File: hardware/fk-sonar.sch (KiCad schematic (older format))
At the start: 46 parts, among them J1 MICRO-USB, J2 Conn_01x03, J3 CONN_01X06, J6 CONN-HDR-2x5, M1 MOUNT_HOLE, M2 MOUNT_HOLE, M3 MOUNT_HOLE, M4 MOUNT_HOLE, Q1 2N7002LT1G, Q2 2N7002LT1G, Q3 2N7002LT1G, Q4 2N7002LT1G, SW1 SPNO, U1 ATSAMD21G18A-AU, U2 MCP1700T-XXX2E, Y1 FC-135

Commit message: Copying fk-core, actually and dropping GPS/SD/etc.
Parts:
- removed D4: PRTR5V0U2X, RocketScreamKicadLibrary:SOT-143B, symbol PRTR5V0U2X
- removed D5: Orange, RocketScreamKicadLibrary:LED-0603, symbol LED-SINGLE
- removed J1: MICRO-USB, conservify:MICRO-USB, symbol MICRO-USB
- removed J2: Conn_01x03, Socket_Strips:Socket_Strip_Straight_1x03_Pitch2.54mm, symbol Conn_01x03
- removed J3: CONN_01X06, Socket_Strips:Socket_Strip_Straight_1x06_Pitch2.54mm, symbol CONN_01X06
- removed J6: CONN-HDR-2x5, Socket_Strips:Socket_Strip_Straight_2x05_Pitch1.27mm_SMD, symbol CONN-HDR-2x5
- removed M2: MOUNT_HOLE, RocketScreamKicadLibrary:HOLE_NPTH_2.2MM, symbol MOUNT_HOLE
- removed U2: MCP1700T-XXX2E, RocketScreamKicadLibrary:SOT-89, symbol MCP1700T-XXX2E
- added C13, C20: 100nF, RocketScreamKicadLibrary:CAP-0603, symbol CAPACITOR-CERAMIC
- added C15, C16: 4.7uF 10V X5R, RocketScreamKicadLibrary:CAP-0603, symbol CAPACITOR-CERAMIC
- added C17, C19, C21: 1uF 10V X5R, RocketScreamKicadLibrary:CAP-0603, symbol CAPACITOR-CERAMIC
- added C18: 10nF, RocketScreamKicadLibrary:CAP-0603, symbol CAPACITOR-CERAMIC
- added D4: Blue, RocketScreamKicadLibrary:LED-0603, symbol LED-SINGLE
- added D5: PMEG3020CPA, RocketScreamKicadLibrary:SOT-1016, symbol DIODE_DUAL_Schottky
- added D6: PRTR5V0U2X, RocketScreamKicadLibrary:SOT-143B, symbol PRTR5V0U2X
- added D7: Green, RocketScreamKicadLibrary:LED-0603, symbol LED-SINGLE
- added D8: Red, RocketScreamKicadLibrary:LED-0603, symbol LED-SINGLE
- added J1: Conn_01x03, Socket_Strips:Socket_Strip_Straight_1x03_Pitch2.54mm, symbol Conn_01x03
- added J2: CONN-HDR-2x5, Socket_Strips:Socket_Strip_Straight_2x05_Pitch1.27mm_SMD, symbol CONN-HDR-2x5
- added J3: RF-SMA-EDGE, RocketScreamKicadLibrary:RF-SMA-EDGE, symbol RF-SMA-EDGE
- added J4: MICRO-USB, RocketScreamKicadLibrary:MICRO-USB, symbol MICRO-USB
- added J5: S2B-PH-SM4-TB, RocketScreamKicadLibrary:S2B-PH-SM4-TB, symbol S2B-PH-SM4-TB
- added M2, M5: FIDUCIAL, RocketScreamKicadLibrary:FIDUCIAL-1MM, symbol FIDUCIAL
- added M6: MOUNT_HOLE, RocketScreamKicadLibrary:HOLE_NPTH_2.2MM, symbol MOUNT_HOLE
- added R11, R6: 2K2, RocketScreamKicadLibrary:RES-0603, symbol RESISTOR
- added R12: 330R, RocketScreamKicadLibrary:RES-0603, symbol RESISTOR
- added R13: 1M, RocketScreamKicadLibrary:RES-0603, symbol RESISTOR
- added R14, R15: 4.7K, RocketScreamKicadLibrary:RES-0603, symbol RESISTOR
- added R16, R18: 10K, RocketScreamKicadLibrary:RES-0603, symbol RESISTOR
- added R19: 1k, RocketScreamKicadLibrary:RES-0603, symbol RESISTOR
- added R20: 180R, RocketScreamKicadLibrary:RES-0603, symbol RESISTOR
- added R7: 1K18, RocketScreamKicadLibrary:RES-0603, symbol RESISTOR
- added U2: RFM95W, RocketScreamKicadLibrary:RFM9xW, symbol RFM9xW
- added U3: BQ24074RGTT, RocketScreamKicadLibrary:QFN-16_3x3mm, symbol BQ24074
- added U4: S25FL116K0XMFI041, RocketScreamKicadLibrary:SOIC-8-N, symbol S25FL1xxK0XM
- added U5: MAX1704XX, Housings_DFN_QFN:DFN-8-1EP_3x2mm_Pitch0.5mm, symbol MAX1704XX
- added U6: MCP1700T-3302E/MB, RocketScreamKicadLibrary:SOT-89, symbol MCP1700T-XXX2E
- C1: value 18pF -> 4.7uF 10V X5R; footprint Capacitors_SMD:C_0603_HandSoldering -> RocketScreamKicadLibrary:CAP-0603; price 0 -> 0.71; spn1 581-06035A180J -> 581-0603ZD475MAT2A
- C10: value 4.7nF -> 4.7uF 10V X5R; footprint Capacitors_SMD:C_0603_HandSoldering -> RocketScreamKicadLibrary:CAP-0603; price 0 -> 0.71; spn1 80-C0603C472K9R -> 581-0603ZD475MAT2A
- C11: value 1uF -> 1uF 50V X5R; footprint Capacitors_SMD:C_0603_HandSoldering -> RocketScreamKicadLibrary:CAP-0603; price 0 -> 0.32
- C12: value 1uF -> 47uF 10V X5R; footprint Capacitors_SMD:C_0603_HandSoldering -> RocketScreamKicadLibrary:CAP-0603; price 0 -> 0.53; spn1 963-UMK107BJ105KA-T -> 81-GRM188R60J476ME5D
- C14: value 4.7uF 10V X5R -> 4.7nF 25V X7R; footprint Capacitors_SMD:C_0603_HandSoldering -> RocketScreamKicadLibrary:CAP-0603; price 0 -> 0.1; spn1 581-0603ZD475MAT2A -> 603-AC603KRX7R8BB472
- C2: value 18pF -> 100nF; footprint Capacitors_SMD:C_0603_HandSoldering -> RocketScreamKicadLibrary:CAP-0603; price 0 -> 0.1; spn1 581-06035A180J -> 81-GRM39X104K50D
- C3, C4: value 100nF -> 18pF; footprint Capacitors_SMD:C_0603_HandSoldering -> RocketScreamKicadLibrary:CAP-0603; price 0 -> 0.1; spn1 81-GRM39X104K50D -> 581-06035A180J
- C5: value 1uF 10V X5R -> 100nF; footprint Capacitors_SMD:C_0603_HandSoldering -> RocketScreamKicadLibrary:CAP-0603; price 0 -> 0.1; spn1 581-0603YD105K -> 81-GRM39X104K50D
- C6: value 100nF -> 1uF 10V X5R; footprint Capacitors_SMD:C_0603_HandSoldering -> RocketScreamKicadLibrary:CAP-0603; price 0 -> 0.1; spn1 81-GRM39X104K50D -> 581-0603YD105K
- C7, C8: footprint Capacitors_SMD:C_0603_HandSoldering -> RocketScreamKicadLibrary:CAP-0603; price 0 -> 0.1
- C9: value 4.7uF -> 100nF; footprint Capacitors_SMD:C_0603_HandSoldering -> RocketScreamKicadLibrary:CAP-0603; price 0 -> 0.1; spn1 581-0603ZD475MAT2A -> 81-GRM39X104K50D
- D1: price 0 -> 0.26
- D2: value Yellow -> Orange; price 0 -> 0.26; spn1 859-LTST-C190KSKT -> 859-LTST-C190KFKT
- D3: value Blue -> Yellow; price 0 -> 0.3; spn1 859-LTST-C191TBKT -> 859-LTST-C190KSKT
- F1: price 0 -> 0.33
- L1, L2: value BLM18KG221SN1D -> BKP1005TS121-T; footprint Inductors_SMD:L_0603_HandSoldering -> RocketScreamKicadLibrary:IND-0603; price 0 -> 0.1; spn1 81-BLM18KG221SN1D -> 963-BKP1608HS121-T
- M1, M3, M4: price 0 -> (none)
- Q1, Q2, Q3, Q4: price 0 -> 0.14
- R1, R17, R5: value 2k2 -> 2K2; footprint Resistors_SMD:R_0603_HandSoldering -> RocketScreamKicadLibrary:RES-0603; price 0 -> 0.1
- R10: value 1M -> 2K94; footprint Resistors_SMD:R_0603_HandSoldering -> RocketScreamKicadLibrary:RES-0603; price 0 -> 0.38; spn1 603-RC0603FR-071ML -> 667-ERJ-S03F2941V
- R2: value 330R -> 10K; footprint Resistors_SMD:R_0603_HandSoldering -> RocketScreamKicadLibrary:RES-0603; price 0 -> 0.1; spn1 603-RC0603FR-07330RL -> 603-RC0603FR-0710KL
- R3: value 2k2 -> 330R; footprint Resistors_SMD:R_0603_HandSoldering -> RocketScreamKicadLibrary:RES-0603; price 0 -> 0.1; spn1 603-RC0603FR-072K2L -> 603-RC0603FR-07330RL
- R4: value 10K -> 2K2; footprint Resistors_SMD:R_0603_HandSoldering -> RocketScreamKicadLibrary:RES-0603; price 0 -> 0.1; spn1 603-RC0603FR-0710KL -> 603-RC0603FR-072K2L
- R8: value 100k -> 46K4; footprint Resistors_SMD:R_0603_HandSoldering -> RocketScreamKicadLibrary:RES-0603; price 0 -> 0.15; spn1 603-RC0603FR-07100KL -> 667-ERJ-3EKF4642V
- R9: value 330R -> 100K; footprint Resistors_SMD:R_0603_HandSoldering -> RocketScreamKicadLibrary:RES-0603; price 0 -> 0.1; spn1 603-RC0603FR-07330RL -> 603-RC0603FR-07100KL
- SW1: footprint RocketScreamKicadLibrary:TS-018 -> conservify:SW_SPST_WURTH_1; price 0 -> 0.55; supplier1 (none) -> digikey
- U1: price 0 -> 3.15
- Y1: price 0 -> 0.54
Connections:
- net labels added: CHG, PG, SD_CS, VBAT, VBUS, VEXT, VIN, WIFI_CS, WIFI_EN, WIFI_IRQ, WIFI_RST, WIFI_WAKE
- net labels removed: SCL2, SCL3, SDA2, SDA3, SENSOR
- wire segments 164 -> 273
- no-connect marks 7 -> 19
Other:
- note added: "1. All capacitors are NP0/COG 50V unless specified.\n2. All resistors are 62.5mW 1% unless specified."
- note added: "100mA"
- note added: "16Mbit = 2Mbytes"
- note added: "500mA"
- note added: "EN2 EN1"
- note added: "FIDUCIALS"
- note added: "HI HI"
- note added: "HI LOW"
- note added: "I-INPUT LIMIT"
- note added: "LED"
- note added: "LEDS"
- note added: "LOW HI"
- note added: "LOW LOW"
- note added: "MCU"
- note added: "MOUNTING"
- note added: "NOTES"
- note added: "POWER MANAGEMENT"
- note added: "RFM95W\n"
- note added: "SERIAL FLASH"
- note added: "SWD/JTAG"
- note added: "Set by R6:1.3A"
- note added: "Standby"
- note added: "USB-DEVICE"
- note added: "VIN:5-10.5V\n(OVP up to 28V)"

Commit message: The PCB.
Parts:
- added J6: Conn_01x04, Socket_Strips:Socket_Strip_Straight_1x04_Pitch2.54mm, symbol Conn_01x04
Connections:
- wire segments 273 -> 279
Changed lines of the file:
@@
 LIBS:conservify
 LIBS:fk-sonar-cache
-LIBS:fk-core-cache
 EELAYER 25 0
 EELAYER END
@@
 RESET
 Text Label 2000 7350 0    50   ~ 0
-D13
+A2
 Text Label 9900 6350 0    50   ~ 0
 USB-
@@
 LEDS
 Text Label 6950 6150 2    50   ~ 0
-A3
+A4
 Text Label 6950 6950 2    50   ~ 0
-A4
+A5
 Text Label 6950 7750 2    50   ~ 0
-A5
+D13
 Wire Wire Line
 	2800 2300 2500 2300
@@
 Wire Wire Line
 	3350 9050 3500 9050
+$Comp
+L Conn_01x04 J6
+U 1 1 5A1E0D62
+P 6450 4100
+F 0 "J6" H 6450 4300 50  0000 C CNN
+F 1 "Conn_01x04" H 6450 3800 50  0000 C CNN
+F 2 "Socket_Strips:Socket_Strip_Straight_1x04_Pitch2.54mm" H 6450 4100 50  0001 C CNN
+F 3 "" H 6450 4100 50  0001 C CNN
+	1    6450 4100
+	1    0    0    -1
+$EndComp
+$Comp
+L 3V3 #PWR069
+U 1 1 5A1E1F21
+P 6100 3950
+F 0 "#PWR069" H 6100 3800 50  0001 C CNN
+F 1 "3V3" H 6100 4090 50  0000 C CNN
+F 2 "" H 6100 3950 60  0000 C CNN
+F 3 "" H 6100 3950 60  0000 C CNN
+	1    6100 3950
+	1    0    0    -1
+$EndComp
+$Comp
+L GND #PWR070
+U 1 1 5A1E2010
+P 6100 4400
+F 0 "#PWR070" H 6100 4150 50  0001 C CNN
+F 1 "GND" H 6100 4250 50  0001 C CNN
+F 2 "" H 6100 4400 60  0000 C CNN
+F 3 "" H 6100 4400 60  0000 C CNN
+	1    6100 4400
+	1    0    0    -1
+$EndComp
+Wire Wire Line
+	6250 4000 6100 4000
+Wire Wire Line
+	6100 4000 6100 3950
+Wire Wire Line
+	6250 4300 6100 4300
+Wire Wire Line
+	6100 4300 6100 4400
+Text Label 6050 4100 0    50   ~ 0
+SDA
+Text Label 6050 4200 0    50   ~ 0
+SCL
+Wire Wire Line
+	6050 4200 6250 4200
+Wire Wire Line
+	6250 4100 6050 4100
 $EndSCHEMATC

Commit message: New SWD/JTAG programming footprint to avoid confusion.
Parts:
- J2: footprint Socket_Strips:Socket_Strip_Straight_2x05_Pitch1.27mm_SMD -> conservify:HDR_2x5_Pitch1.27mm_SMD_JTAG_SWD
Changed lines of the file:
@@
 F 0 "J2" H 6050 10250 60  0000 C CNN
 F 1 "CONN-HDR-2x5" H 6050 9500 60  0001 C CNN
-F 2 "Socket_Strips:Socket_Strip_Straight_2x05_Pitch1.27mm_SMD" H 6050 9400 60  0001 C CNN
+F 2 "conservify:HDR_2x5_Pitch1.27mm_SMD_JTAG_SWD" H 6050 9400 60  0001 C CNN
 F 3 "" H 6050 9750 60  0000 C CNN
 F 4 "0.73" H 6050 10350 50  0001 C CNN "price"

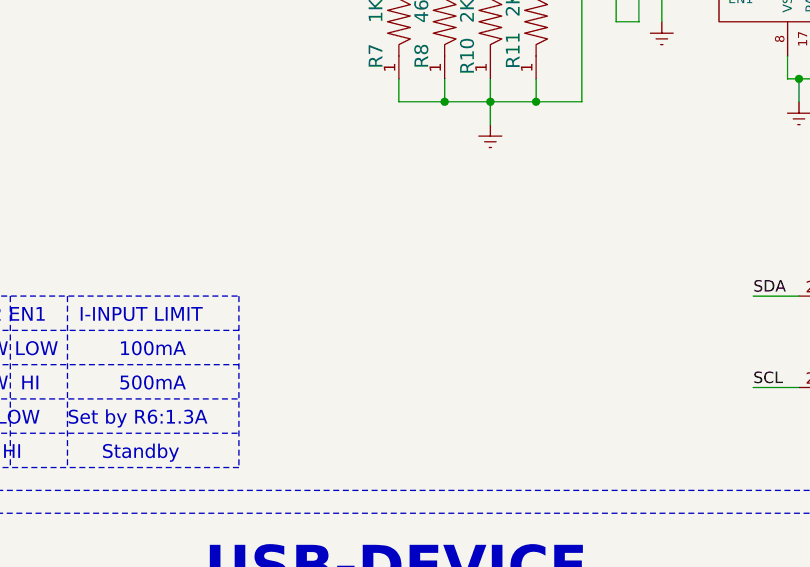
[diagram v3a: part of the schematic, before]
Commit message: Adding a solar panel connector. Just a JST below the battery JST.
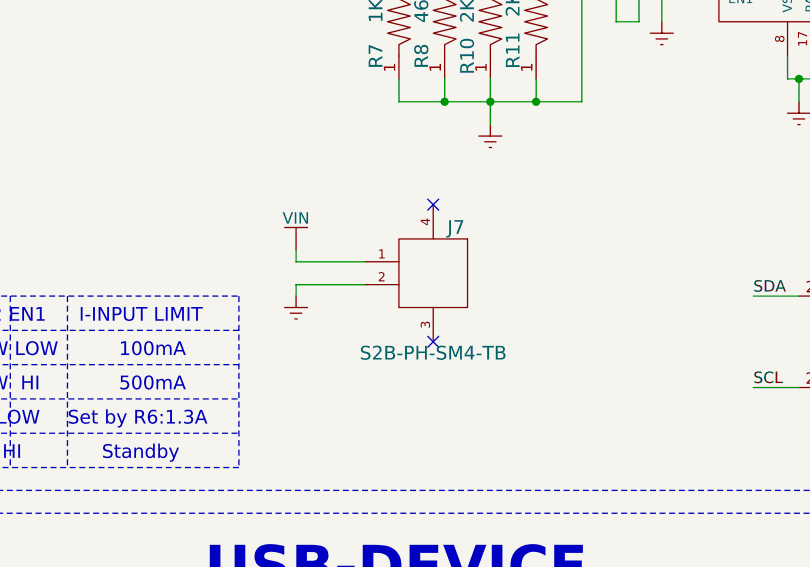
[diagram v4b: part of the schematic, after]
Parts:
- added J7: S2B-PH-SM4-TB, RocketScreamKicadLibrary:S2B-PH-SM4-TB, symbol S2B-PH-SM4-TB
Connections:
- wire segments 279 -> 283
- no-connect marks 19 -> 21
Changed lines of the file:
@@
 Wire Wire Line
 	6250 4100 6050 4100
+$Comp
+L VIN #PWR071
+U 1 1 5A39857F
+P 8900 4050
+F 0 "#PWR071" H 8900 3900 50  0001 C CNN
+F 1 "VIN" H 8900 4190 50  0000 C CNN
+F 2 "" H 8900 4050 60  0000 C CNN
+F 3 "" H 8900 4050 60  0000 C CNN
+	1    8900 4050
+	1    0    0    -1
+$EndComp
+$Comp
+L GND #PWR072
+U 1 1 5A39866E
+P 8900 4250
+F 0 "#PWR072" H 8900 4000 50  0001 C CNN
+F 1 "GND" H 8900 4100 50  0001 C CNN
+F 2 "" H 8900 4250 60  0000 C CNN
+F 3 "" H 8900 4250 60  0000 C CNN
+	1    8900 4250
+	1    0    0    -1
+$EndComp
+$Comp
+L S2B-PH-SM4-TB J7
+U 1 1 5A398760
+P 9500 4150
+F 0 "J7" H 9400 4350 60  0000 C CNN
+F 1 "S2B-PH-SM4-TB" H 9500 3800 60  0000 C CNN
+F 2 "RocketScreamKicadLibrary:S2B-PH-SM4-TB" H 9500 3700 60  0001 C CNN
+F 3 "" H 9450 4150 60  0000 C CNN
+F 4 "0.58" H 9400 4450 50  0001 C CNN "price"
+F 5 "455-1749-1-ND" H -3150 1350 50  0001 C CNN "spn1"
+F 6 "digikey" H -3150 1350 50  0001 C CNN "supplier1"
+	1    9500 4150
+	-1   0    0    -1
+$EndComp
+NoConn ~ 9500 3850
+NoConn ~ 9500 4450
+Wire Wire Line
+	9200 4100 8900 4100
+Wire Wire Line
+	8900 4100 8900 4050
+Wire Wire Line
+	8900 4250 8900 4200
+Wire Wire Line
+	8900 4200 9200 4200
 $EndSCHEMATC

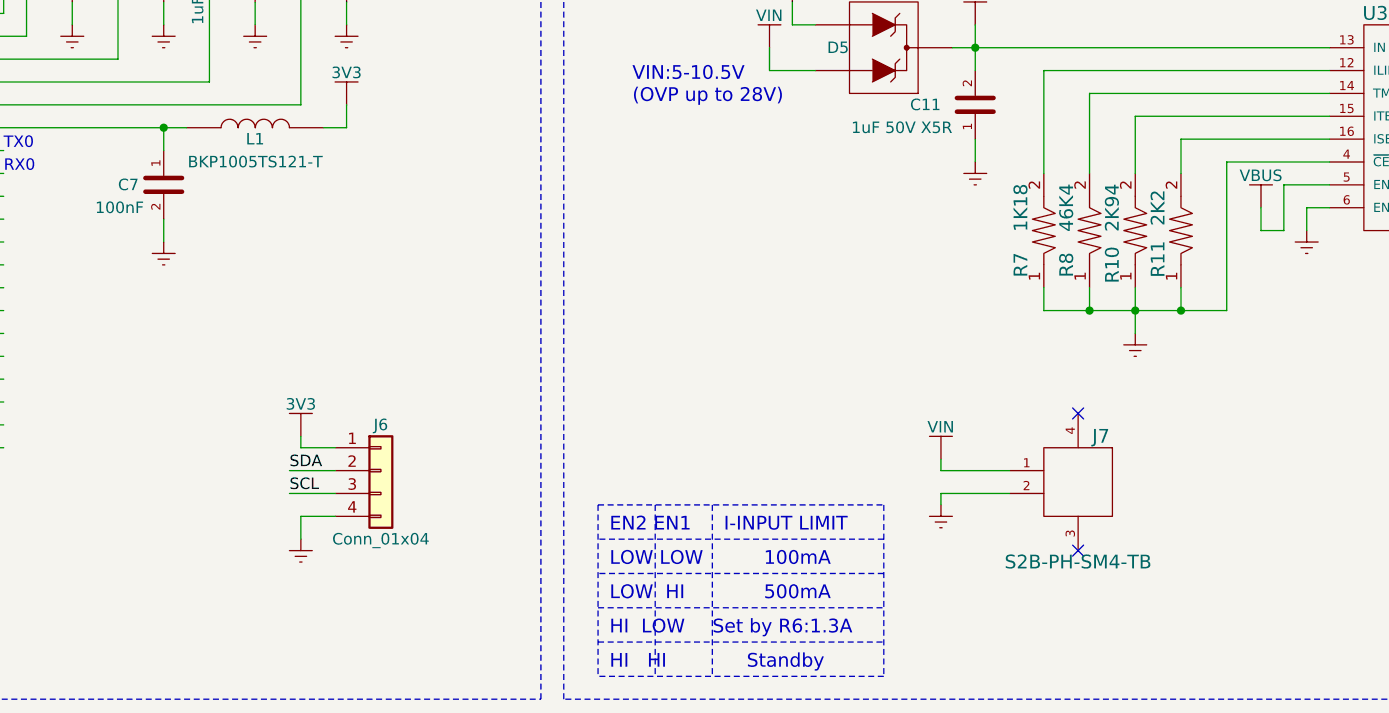
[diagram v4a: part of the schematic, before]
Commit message: Labels on SDA/SCL header. Also made GND the square pad.
No room for the label there.
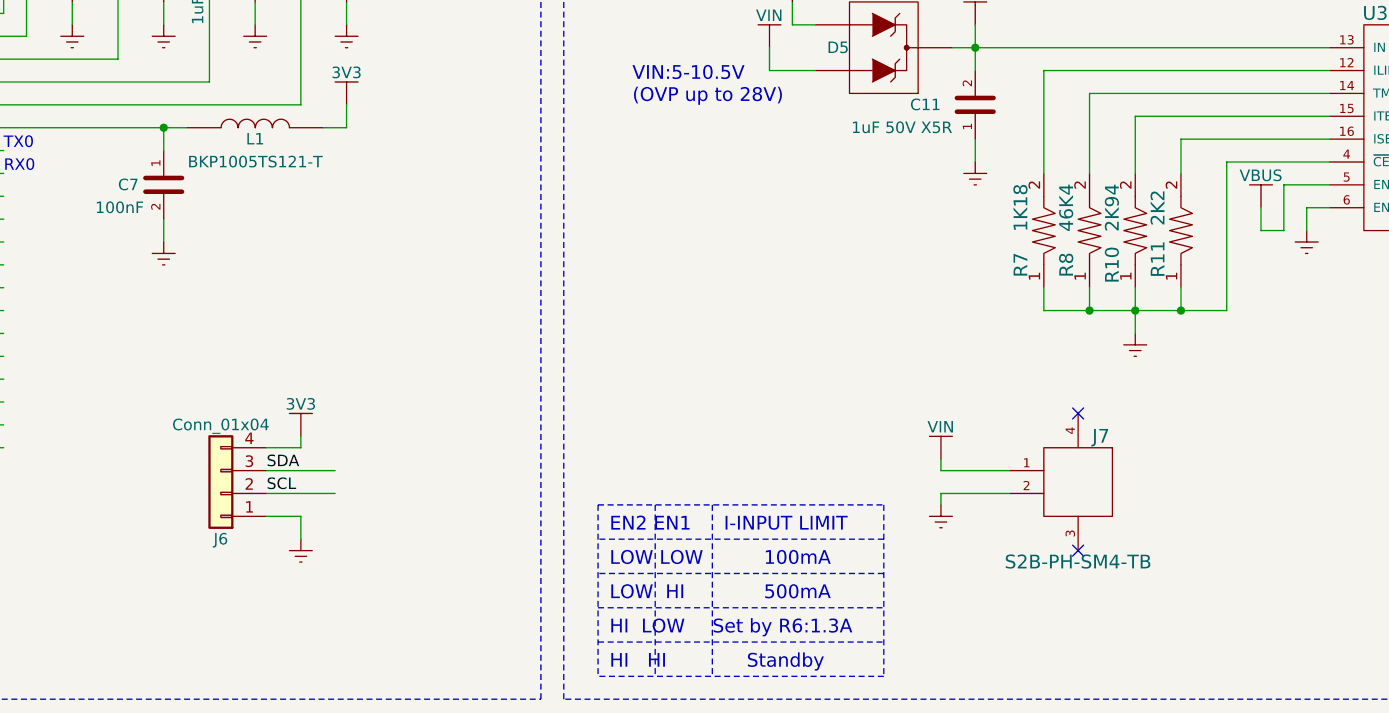
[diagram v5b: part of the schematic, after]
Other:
- moved on the sheet: J6
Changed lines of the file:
@@
 	10600 2750 10150 2750
 Wire Wire Line
-	10150 2750 10150 3400
-Wire Wire Line
-	10150 3400 9350 3400
+	10150 3400 10150 2750
+Wire Wire Line
+	9350 3400 10150 3400
 Wire Wire Line
 	9950 3400 9950 3300
@@
 L Conn_01x04 J6
 U 1 1 5A1E0D62
-P 6450 4100
-F 0 "J6" H 6450 4300 50  0000 C CNN
-F 1 "Conn_01x04" H 6450 3800 50  0000 C CNN
-F 2 "Socket_Strips:Socket_Strip_Straight_1x04_Pitch2.54mm" H 6450 4100 50  0001 C CNN
-F 3 "" H 6450 4100 50  0001 C CNN
-	1    6450 4100
-	1    0    0    -1
+P 5750 4200
+F 0 "J6" H 5750 4400 50  0000 C CNN
+F 1 "Conn_01x04" H 5750 3900 50  0000 C CNN
+F 2 "Socket_Strips:Socket_Strip_Straight_1x04_Pitch2.54mm" H 5750 4200 50  0001 C CNN
+F 3 "" H 5750 4200 50  0001 C CNN
+	1    5750 4200
+	-1   0    0    1
 $EndComp
 $Comp
@@
 $EndComp
 Wire Wire Line
-	6250 4000 6100 4000
+	5950 4000 6100 4000
 Wire Wire Line
 	6100 4000 6100 3950
 Wire Wire Line
-	6250 4300 6100 4300
+	5950 4300 6100 4300
 Wire Wire Line
 	6100 4300 6100 4400
-Text Label 6050 4100 0    50   ~ 0
+Text Label 5950 4100 0    50   ~ 0
 SDA
-Text Label 6050 4200 0    50   ~ 0
+Text Label 5950 4200 0    50   ~ 0
 SCL
 Wire Wire Line
-	6050 4200 6250 4200
-Wire Wire Line
-	6250 4100 6050 4100
+	5950 4200 6250 4200
+Wire Wire Line
+	6250 4100 5950 4100
 $Comp
 L VIN #PWR071

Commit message: Just some cleanup. Fix the fuel gauge lines.
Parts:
- added R21, R22: 4.7K, RocketScreamKicadLibrary:RES-0603, symbol RESISTOR
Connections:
- net labels added: FLASH_CS, RADIO_CS, RADIO_D0, SCL1, SCL3, SDA1, SDA3
- net labels removed: ATN, D2, D3, D4, D5, D6, SCL, SDA
- wire segments 283 -> 288
- no-connect marks 21 -> 19
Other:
- note removed: "RX1"
- note removed: "TX1"
- moved on the sheet: C17, C18, J3, R19, R20, U5

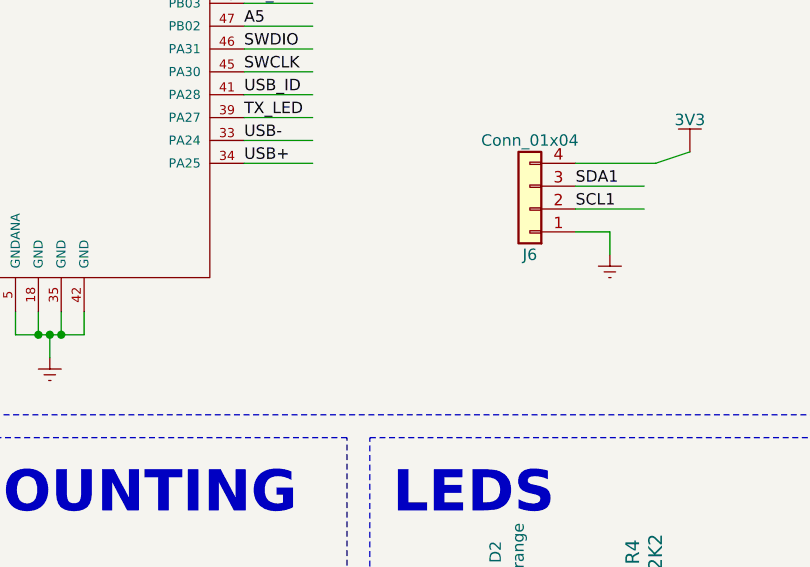
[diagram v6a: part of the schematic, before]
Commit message: Exposing D30/D31 (as test points because stuff is kind of cramped)
If this becomes more regular/useful I'll make them pins or use a header.
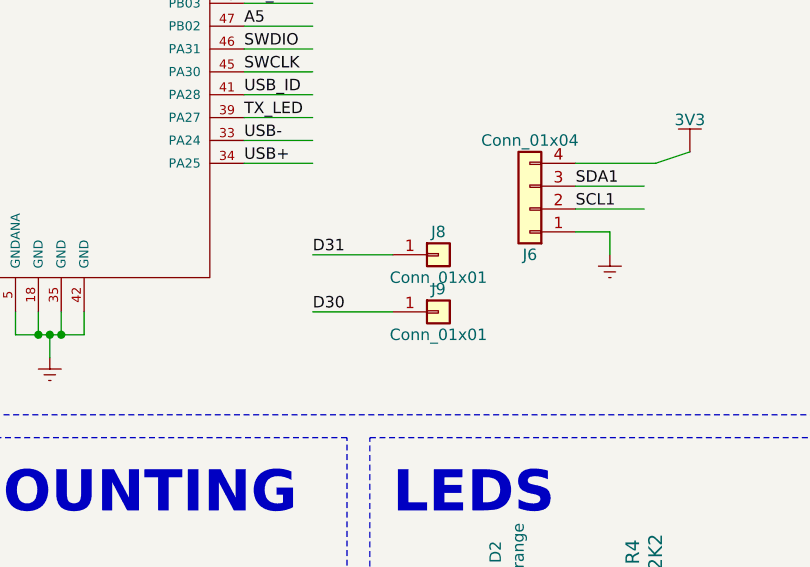
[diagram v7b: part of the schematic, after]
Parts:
- added J8, J9: Conn_01x01, Measurement_Points:Measurement_Point_Round-SMD-Pad_Small, symbol Conn_01x01
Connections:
- wire segments 288 -> 290

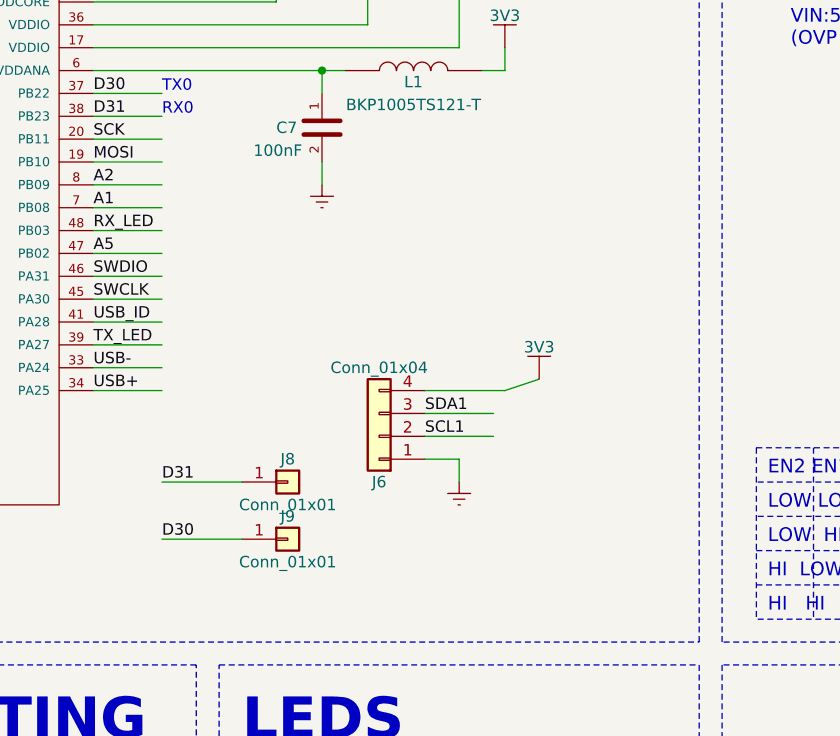
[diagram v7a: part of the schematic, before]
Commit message: Fix USB footprint. Add a Molex for D30/D31 serial.
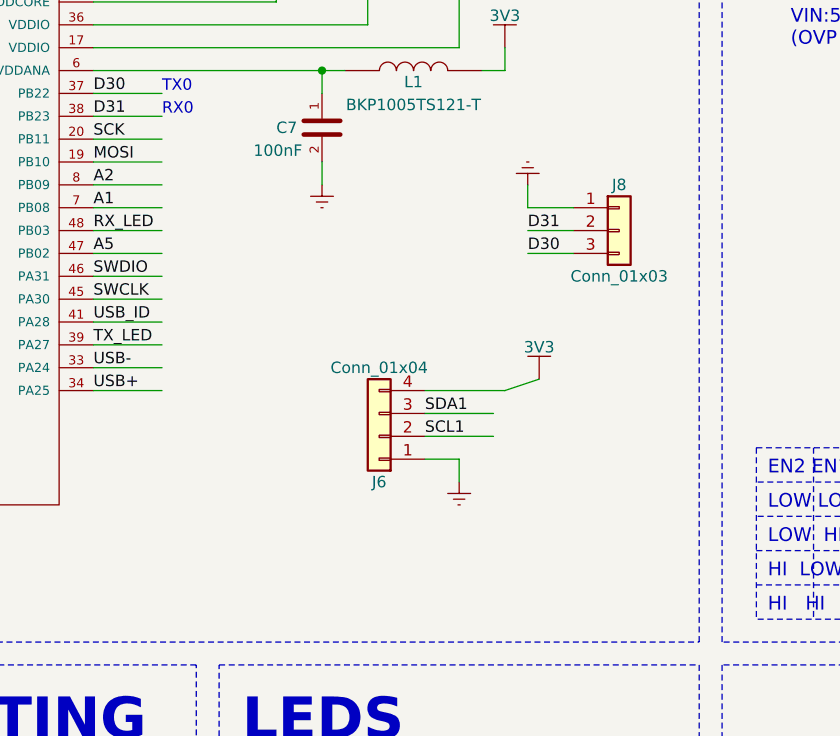
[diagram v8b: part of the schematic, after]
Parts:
- removed J8, J9: Conn_01x01, Measurement_Points:Measurement_Point_Round-SMD-Pad_Small, symbol Conn_01x01
- added J8: Conn_01x03, conservify:Molex_CLIK-Mate_502382-0370_1x03_P1.25mm_Vertical, symbol Conn_01x03
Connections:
- wire segments 290 -> 292
